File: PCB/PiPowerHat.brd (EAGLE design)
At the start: 65 x 56 mm, 35 parts, among them IC1 7805T, K1 PIN20X2, U1 EEPROM24, U2 INA219AIDCNRSOIC, U4 DS18B20, U5 DS1820SOIC

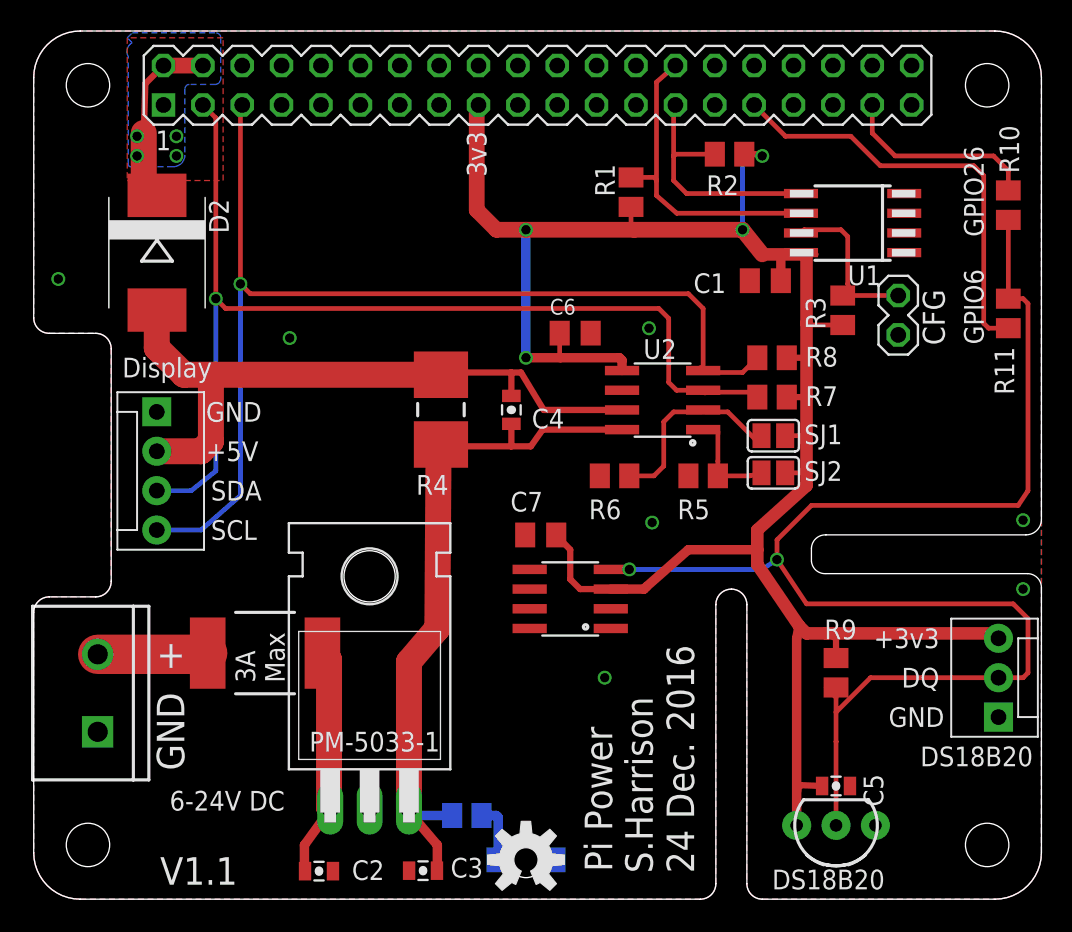
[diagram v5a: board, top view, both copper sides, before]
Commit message: Changed 7805 style regulator to the 3A buck regulator.
Added DotStar LED strip connector (clk/data).

Added 2 GPIO port + power connector.

Added 2x fan connectors (1x 4 pin PWM, 1x 3 pin PWM power)

Added fuse.

Moved current/voltage sensor to pre-regulator to monitor the input voltage.

Moved board temperature sensor to be under regulator module.
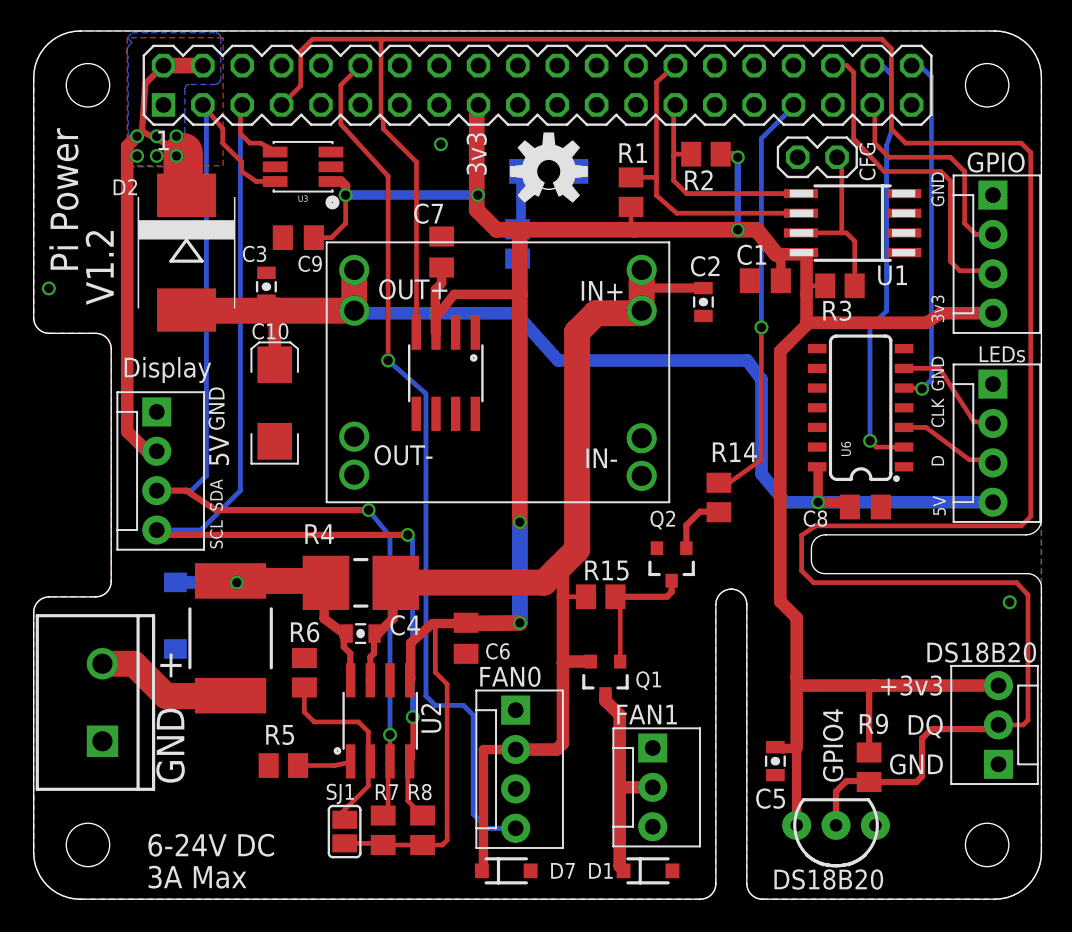
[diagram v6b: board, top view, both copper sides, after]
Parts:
- removed IC1: 7805T, linear:TO220H
- removed R10, R11: 0R, resistor:M0805
- removed SJ2: (no value), jumper:SJ
- added C10: 10UF, SparkFun-Capacitors:EIA6032-NOM
- added C8, C9: 100nF, resistor:C0805K
- added D1, D7: (no value), SparkFun-DiscreteSemi:SOD-123
- added D6: B340A, SparkFun-DiscreteSemi:SMA-DIODE
- added J4: FAN1, SparkFun-Connectors:MOLEX-1X3
- added JP1: LEDs, SparkFun-Connectors:MOLEX-1X4
- added JP2: FAN0, SparkFun-Connectors:MOLEX-1X4
- added JP4: GPIO, SparkFun-Connectors:MOLEX-1X4
- added Q1: NX2301P, SparkFun-DiscreteSemi:SOT23-3
- added Q2: (no value), SparkFun-DiscreteSemi:SOT23-3
- added R14, R15: 10k, resistor:M0805
- added U$1: MINI-BUCK-MODULE-3A, Tinamous:MINI-BUCK-MODULE-3A
- added U3: TSL2561T, SparkFun-Sensors:TMB-6
- added U6: 74AC125, SparkFun-DigitalIC:SO14
- D2: value (none) -> MBRS340T3G
- J3: value (none) -> Display
- moved D3 44.4 mm to (33.2, 46.9)
- moved LOGO1 44.4 mm to (33.2, 46.9)
- moved C2 44.3 mm to (43.2, 38.5), turned to 90 degrees
- moved C3 39.0 mm to (15.0, 39.5), turned to 270 degrees
- moved R8 37.9 mm to (25.1, 4.45), turned to 270 degrees
- moved SJ1 37.6 mm to (20.1, 4.36), turned to 90 degrees
- moved R7 37.5 mm to (22.5, 4.45), turned to 270 degrees
- moved R12 37.0 mm to (31.2, 42.3), turned to 270 degrees
- moved R5 32.9 mm to (16.1, 8.62)
- moved U2 27.6 mm to (22.4, 11.5), turned to 0 degrees
- moved R6 23.7 mm to (17.5, 14.6), turned to 270 degrees
- moved C6 20.9 mm to (27.9, 16.8), turned to 270 degrees
- moved C7 19.3 mm to (26.3, 41.7), turned to 90 degrees
- moved C4 17.4 mm to (21.1, 17.1), turned to 180 degrees
- moved U5 16.6 mm to (26.6, 33.9), turned to 180 degrees
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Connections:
- net N$1 renamed DC_IN
- removed net GPIO4: K1.7
- removed net GPIO6: K1.31, R11.2
- removed net N$2: D2.C, K1.2, K1.4
- removed net VCC: C3.2, C4.2, IC1.3, R12.2, R4.2, U2.8
- new net DOTSTAR_CLOCK: JP1.2, U6.6
- new net DOTSTAR_DATA: JP1.3, U6.3
- new net FAN0_PWM: JP2.4, K1.12
- new net FAN1_PWM: K1.33, R14.2
- new net GPIO16: JP4.3, K1.36
- new net LED_MOSI: K1.38, U6.2
- new net LED_SCLK: K1.40, U6.5
- new net N$13: Q2.1, R14.1
- new net N$5: C4.2, D6.C, F1.2, R4.2, U2.8
- new net N$7: D1.C, J4.2, Q1.3
- new net N$8: Q1.1, Q2.3, R15.1
- new net PI_5V: D2.C, J3.2, K1.2, K1.4
- net +3V3: now also C9.1, JP4.4, U3.1; no longer K1.1, SJ2.1
- net +5V: now also C10.A, C3.2, C8.1, JP1.4, R12.2, U$1.OUT@1, U$1.OUT@2, U6.14; no longer C4.1, J3.2, R4.1, U2.7
- net GND: now also C10.C, C8.2, C9.2, D1.A, D6.A, D7.A, J4.1, JP1.1, JP2.1, JP4.1, Q2.2, U$1.GND@1, U$1.GND@2, U$1.GND@3, U$1.GND@4, U3.2, U3.3, U6.1, U6.10, U6.12, U6.13, U6.4, U6.7, U6.9; no longer IC1.2
- net GPIO26: now also JP4.2; no longer R10.2
- net N$10: no longer SJ2.2
- net SCL: now also U3.4
- net SDA: now also U3.6
- net TEMPERATURE: now also K1.7; no longer R10.1, R11.1
- net VIN: now also C4.1, D7.C, JP2.2, Q1.2, R15.2, R4.1, U$1.IN@1, U$1.IN@2, U2.7; no longer F1.2, IC1.1
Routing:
- net TEMPERATURE: track 93.2 -> 159.7 mm, vias 2 -> 0
- net VIN: track 14.8 -> 73.4 mm
- net FAN0_PWM: track 0.00 -> 56.5 mm, vias 0 -> 1
- net +3V3: track 142.2 -> 198.5 mm, vias 4 -> 6
- net VCC: track 45.5 -> 0.00 mm
- net +5V: track 44.3 -> 81.2 mm, vias 0 -> 1
- net PI_5V: track 0.00 -> 34.8 mm, vias 0 -> 6
- net LED_MOSI: track 0.00 -> 28.0 mm, vias 0 -> 1
- net GPIO6: track 27.9 -> 0.00 mm
- net FAN1_PWM: track 0.00 -> 27.0 mm, vias 0 -> 1
- net LED_SCLK: track 0.00 -> 23.1 mm, vias 0 -> 1
- net GPIO16: track 0.00 -> 21.5 mm
- net N$5: track 0.00 -> 18.3 mm, vias 0 -> 1
- net N$7: track 0.00 -> 14.1 mm
- net N$2: track 12.2 -> 0.00 mm, vias 4 -> 0
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- added copper zone on layer 1, net PI_5V
- added copper zone on layer 16, net PI_5V
- removed copper zone on layer 1, net N$2
- removed copper zone on layer 16, net N$2
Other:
- board text added: "5V"
- board text added: "CLK"
- board text added: "D"
- board text added: "FAN0"
- board text added: "FAN1"
- board text added: "GPIO"
- board text added: "GPIO4"
- board text added: "LEDs"
- board text added: "S.Harrison 27 Feb 2017"
- board text added: "V1.2"
- board text removed: "+5V"
- board text removed: "GPIO26"
- board text removed: "GPIO6"
- board text removed: "PM-5033-1"
- board text removed: "S.Harrison 24 Dec. 2016"
- board text removed: "V1.1"

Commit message: Added some improvements...
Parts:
- removed R5: 10k, resistor:M0805
- added JP3: (no value), SparkFun-Connectors:MOLEX-1X2
- added JP5: (no value), SparkFun-Connectors:1X05
- added SURVO-0, SURVO-1: (no value), SparkFun-Connectors:1X03
- J3: device SparkFun-Connectors:MOLEX-1X4 -> SparkFun-Connectors:MOLEX-1X6
- moved U3 44.7 mm to (27.1, 3.66)
- moved C9 41.4 mm to (21.3, 1.52)
- moved SJ1 11.7 mm to (28.6, 12.4), turned to 180 degrees
- moved C2 8.30 mm to (35.2, 40.6), turned to 0 degrees
- moved R7 8.16 mm to (28.5, 10.0), turned to 0 degrees
- moved C3 7.55 mm to (20.5, 44.7)
- moved D6 5.60 mm to (13.1, 14.3)
- moved Q1 5.49 mm to (41.5, 17.4), turned to 270 degrees
- moved R8 4.71 mm to (28.5, 7.71), turned to 0 degrees
- moved J3 3.35 mm to (7.94, 34.8)
- moved R6 3.33 mm to (18.4, 11.4)
- moved C1 3.28 mm to (43.9, 39.6), turned to 270 degrees
- moved D7 3.05 mm to (33.5, 1.83), turned to 180 degrees
- moved Q2 2.89 mm to (38.4, 22.6)
- moved R14 2.81 mm to (42.4, 23.8)
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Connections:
- net ID_SD renamed ID_SDA
- removed net N$10: R5.2, U2.1
- new net BCM10_MOSI: JP5.4, K1.19
- new net BCM11_SCLK: JP5.2, K1.23
- new net BCM14_TXD: K1.8
- new net BCM15_RXD: K1.10
- new net BCM22: K1.15
- new net BCM5: K1.29
- new net BCM8_CE0: K1.24
- new net BCM9_MISO: JP5.3, K1.21
- new net N$1: K1.18
- new net NFC_INT: J3.6, K1.13
- new net NFC_RESET: J3.5, K1.11
- new net SURVO_0: SURVO-0.2, U6.8
- new net SURVO_0_PWM: K1.31, U6.9
- new net SURVO_1: SURVO-1.2, U6.11
- new net SURVO_1_PWM: K1.32, U6.12
- net +3V3: now also J3.2, JP5.5
- net +5V: now also SURVO-0.3, SURVO-1.3
- net GND: now also JP3.1, JP5.1, SURVO-0.1, SURVO-1.1, U2.1; no longer R5.1, U6.12, U6.9
- net PI_5V: now also JP3.2; no longer J3.2
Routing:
- net NFC_INT: track 0.00 -> 42.1 mm
- net NFC_RESET: track 0.00 -> 37.1 mm
- net SURVO_1_PWM: track 0.00 -> 35.0 mm, vias 0 -> 1
- net SURVO_0_PWM: track 0.00 -> 24.7 mm, vias 0 -> 1
- net +3V3: track 198.5 -> 219.7 mm, vias 6 -> 5
- net +5V: track 81.2 -> 98.4 mm
- net PI_5V: track 34.8 -> 20.5 mm, vias 6 -> 3
- net SURVO_0: track 0.00 -> 9.84 mm
- net VIN: track 73.4 -> 81.9 mm
- net N$9: track 12.9 -> 17.9 mm
- net N$10: track 4.89 -> 0.00 mm
- net SCL: track 71.0 -> 75.8 mm
- net FAN1_PWM: track 27.0 -> 31.6 mm
- net N$8: track 8.78 -> 4.90 mm
- net SURVO_1: track 0.00 -> 3.65 mm
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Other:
- board text added: "16"
- board text added: "26"
- board text added: "NFC IRQ"
- board text added: "NFC RESET"
- board text added: "V1.3"
- board text removed: "V1.2"
